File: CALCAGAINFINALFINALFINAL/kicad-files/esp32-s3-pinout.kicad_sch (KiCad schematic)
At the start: 1 part, among them U8 ESP32-S3-WROOM-1

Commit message: added 11pin expansion for accessories and micro-sd card slot
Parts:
- added H1, H2, H3, H4, H5: MountingHole_Pad, MountingHole:MountingHole_2.5mm_Pad, symbol Mechanical:MountingHole_Pad
- added J1: Conn_01x11_Socket, Connector_JST:JST_EH_B11B-EH-A_1x11_P2.50mm_Vertical, symbol Connector:Conn_01x11_Socket
- added J3: Micro_SD_Card, Connector_Card:microSD_HC_Molex_47219-2001, symbol Connector:Micro_SD_Card
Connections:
- net 3V3: now also J1.2 (Pin_2)
- net CS: now also H3.1
- net DC: now also H5.1
- net MOSI: now also H1.1, J1.6 (Pin_6)
- net RST: now also H4.1
- net SCK: now also H2.1, J1.8 (Pin_8)
- net SCL: now also J1.5 (Pin_5)
- net SDA: now also J1.4 (Pin_4)
- net GND: now reaches U8.1 (GND), U8.40 (GND), U8.41 (GND)
- net GND: now also J1.1 (Pin_1), J3.6 (VSS)
- net extra: now reaches U8.12 (IO8)
- net extra: now also J1.11 (Pin_11)
- net ~{INT}: now reaches U8.19 (IO11)
- net MISO: now reaches U8.22 (IO14)
- net MISO: now also J1.7 (Pin_7)
- net CS1: now reaches U8.8 (IO15)
- net CS1: now also J1.9 (Pin_9)
- net ~{INT1}: now reaches U8.9 (IO16)
- net ~{INT1}: now also J1.10 (Pin_10)
- new net VCC: J1.3 (Pin_3), J3.4 (VDD)
- no-connect marks 0 -> 1
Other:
- note added: "================================ J1 11-PIN EXPANSION PORT NOTES ================================ PINOUT MAPPING: - P1: GND | P7: MISO (IO14) [SPI Shared] - P2: 3V3 | P8: SCK (IO12) [SPI Shared] - P3: 5V (VBUS) | P9: CS1 (IO15) [Dedicated] - P4: SDA (IO7) | P10: IRQ (IO16) [Dedicated] - P5: SCL (IO6) | P11: TX (IO8) [Dedicated] - P6: MOSI(IO13) DESIGN & COEXISTENCE RULES: - SPI: Shares MOSI/SCK wi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"
- note added: "Display pins"

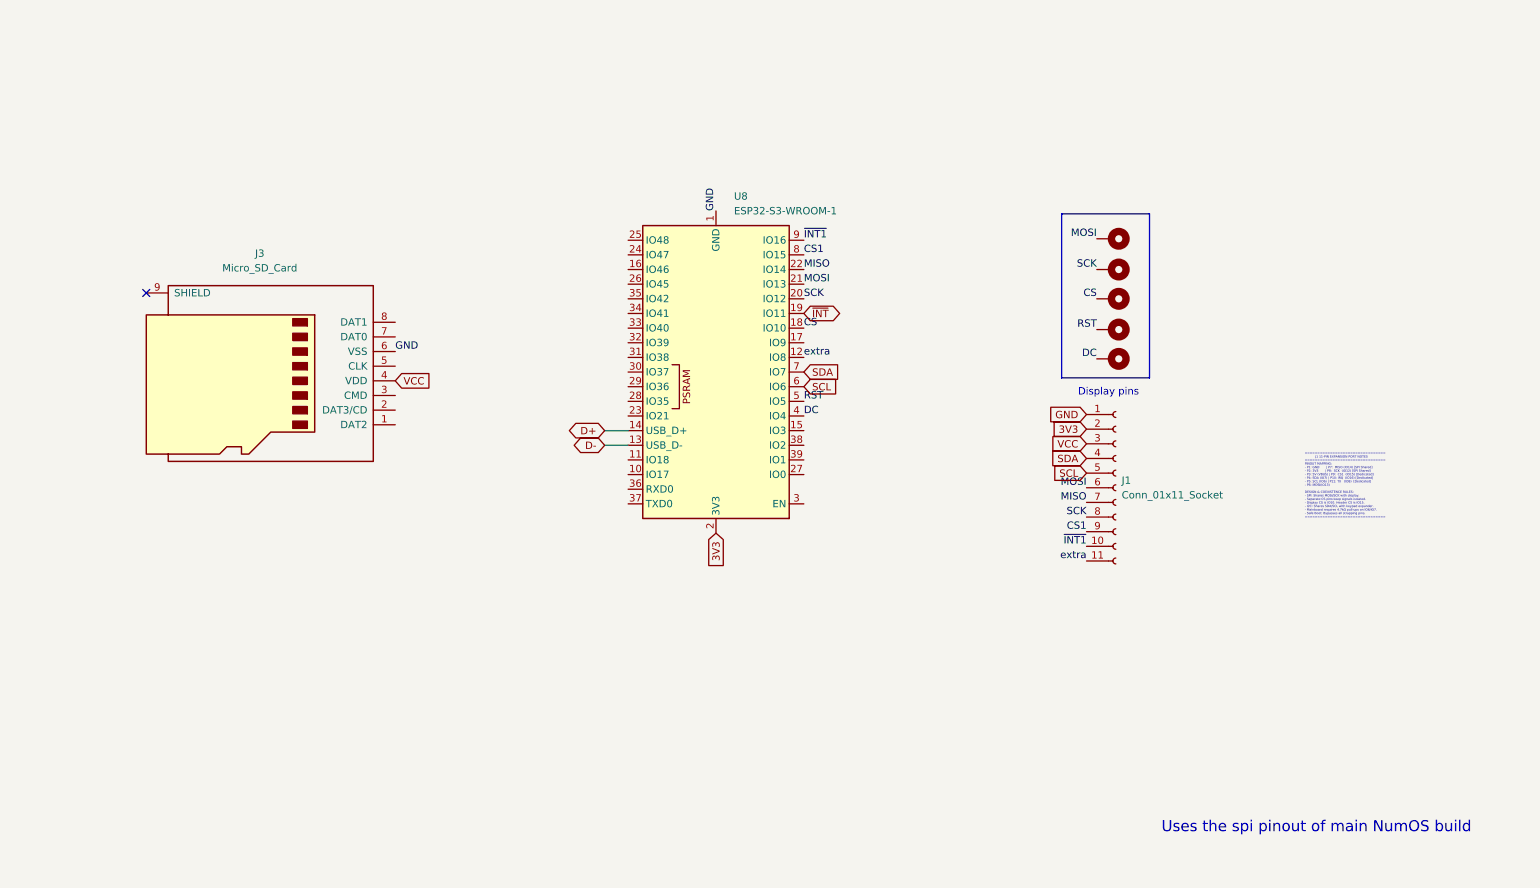
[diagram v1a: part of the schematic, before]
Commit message: Finished SD card and screen. Added camera connector and adjacent gpio expander
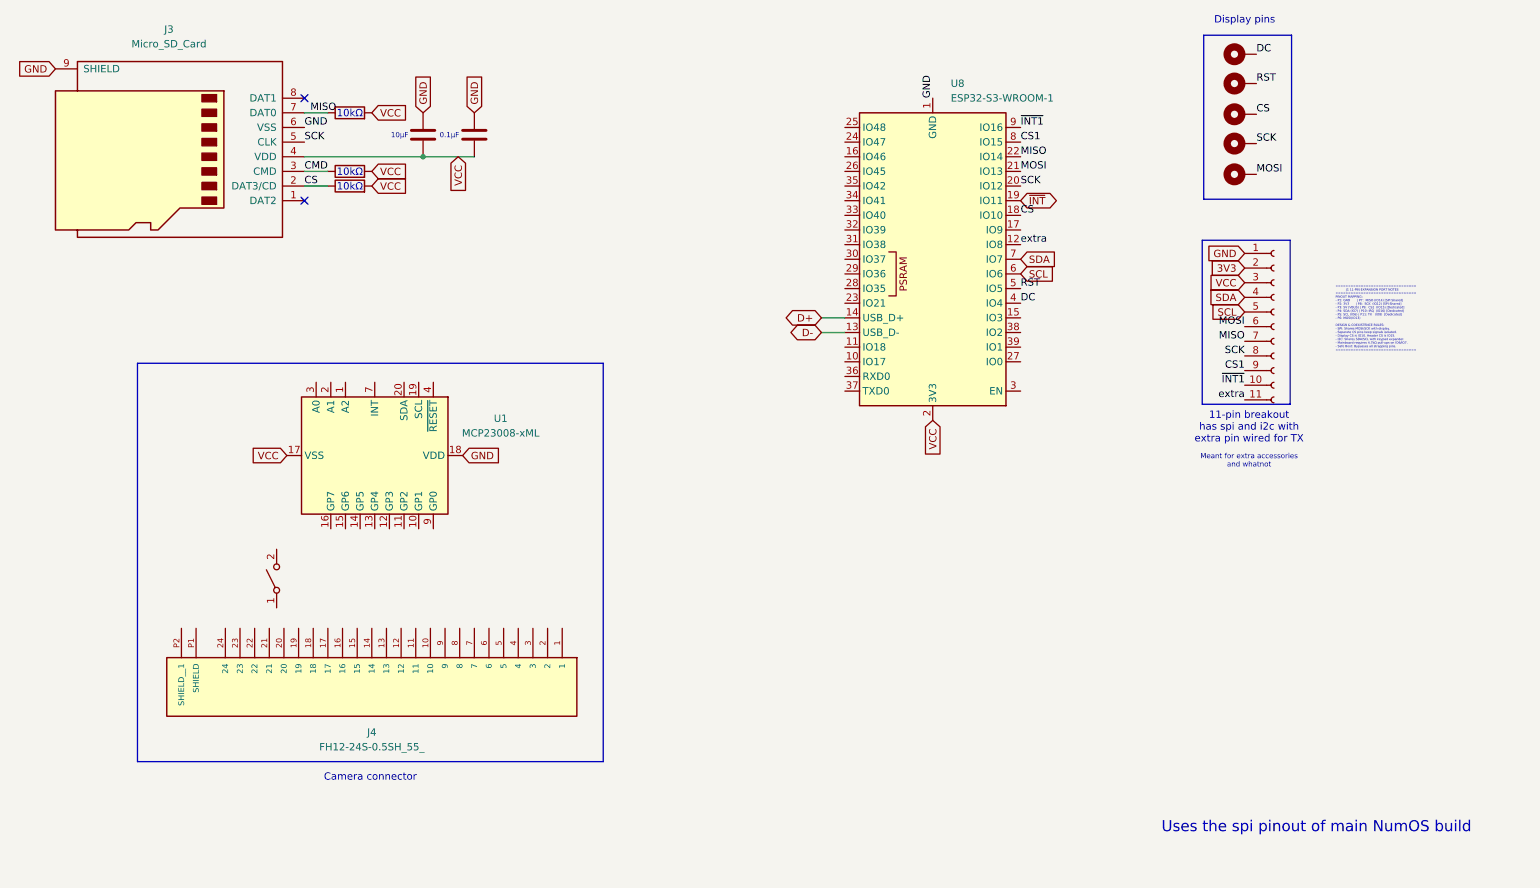
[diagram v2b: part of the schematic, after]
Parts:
- added C1, C2: C, symbol Device:C
- added J4: FH12-24S-0.5SH_55_, FH12-24S-0.5SH_55_:HRS_FH12-24S-0.5SH_55_, symbol FH12-24S-0.5SH_55_:FH12-24S-0.5SH_55_
- added R1, R2, R3: R, symbol Device:R
- added SW1: SW_SPST, symbol Switch:SW_SPST
- added U1: MCP23008-xML, Package_DFN_QFN:QFN-20-1EP_4x4mm_P0.5mm_EP2.7x2.7mm, symbol Interface_Expansion:MCP23008-xML
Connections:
- net 3V3: no longer U8.2 (3V3)
- net CS: now also J3.2 (DAT3/CD), R3.1
- net GND: now also J3.9 (SHIELD), C1.2, C2.2, U1.18 (VDD)
- net MISO: now also J3.7 (DAT0), R2.1
- net SCK: now also J3.5 (CLK)
- net VCC: now also U8.2 (3V3), C1.1, C2.1, R1.2, R2.2, R3.2, U1.17 (VSS)
- net CMD: now reaches J3.3 (CMD)
- net CMD: now also R1.1
- no-connect marks 1 -> 2
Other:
- note added: "0.1µF"
- note added: "10kΩ"
- note added: "10µF"
- note added: "11-pin breakout has spi and i2c with extra pin wired for TX"
- note added: "Camera connector"
- note added: "Meant for extra accessories and whatnot"
- moved on the sheet: J3, U8

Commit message: nearly finished with the no camera variant schematic stil have 2 drc warnings to fix but should be done in the next few hours.
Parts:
- removed J4: FH12-24S-0.5SH_55_, FH12-24S-0.5SH_55_:HRS_FH12-24S-0.5SH_55_, symbol FH12-24S-0.5SH_55_:FH12-24S-0.5SH_55_
- removed SW1: SW_SPST, symbol Switch:SW_SPST
- removed U1: MCP23008-xML, Package_DFN_QFN:QFN-20-1EP_4x4mm_P0.5mm_EP2.7x2.7mm, symbol Interface_Expansion:MCP23008-xML
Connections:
- net GND: now also J3.SH (SHIELD); no longer J3.9 (SHIELD)
- no-connect marks 2 -> 25
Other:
- note added: "SD card Slot"
- note added: "pin header for extra accessories and whatnot"
- note removed: "Camera connector"
- note removed: "Meant for extra accessories and whatnot"
- note removed: "Uses the spi pinout of main NumOS build"
- moved on the sheet: U8

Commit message: finalised no-camera branch. designing pcb then committing to origin/no-camera then tracing and adding camera to main
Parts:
- C1, C2: footprint (none) -> Capacitor_SMD:CP_Elec_3x5.3
- R1, R2, R3: footprint (none) -> Resistor_SMD:R_0201_0603Metric
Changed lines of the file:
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@@
 			)
 		)
-		(property "Footprint" ""
+		(property "Footprint" "Resistor_SMD:R_0201_0603Metric"
 			(at 77.724 47.244 90)
 			(hide yes)
@@
 			)
 		)
-		(property "Footprint" ""
+		(property "Footprint" "Capacitor_SMD:CP_Elec_3x5.3"
 			(at 98.3488 35.306 0)
 			(hide yes)
@@
 			)
 		)
-		(property "Footprint" ""
+		(property "Footprint" "Capacitor_SMD:CP_Elec_3x5.3"
 			(at 89.4588 35.306 0)
 			(hide yes)
@@
 			)
 		)
-		(property "Footprint" ""
+		(property "Footprint" "Resistor_SMD:R_0201_0603Metric"
 			(at 77.724 37.084 90)
 			(hide yes)
@@
 			)
 		)
-		(property "Footprint" ""
+		(property "Footprint" "Resistor_SMD:R_0201_0603Metric"
 			(at 77.724 49.784 90)
 			(hide yes)

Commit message: dude this bitch ass project is the fucking boulder of sisyphus omfg ima genuinely kms at this rate if this iteration doesnt work ima genuinely kms like acutal this one is bare esp32 s3 with a diy antenna and crystal like dude what the actual fuck man ima genuinely dei. FINAL FINAL FINAL FINAL ITS GOT THE FUCKING BARE CHIPS FOR DAMN NEAR EVERYTHING DEAR MASS PRODUCED CHINK FACTORY GODS LET THIS THROUGH WITHOUT CAUSING A RUCKUS AND CHARGING LIKE $90 FOR 14 BUCKS OF PARTS AMEN
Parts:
- removed J1: Conn_01x11_Socket, Connector_JST:JST_EH_B11B-EH-A_1x11_P2.50mm_Vertical, symbol Connector:Conn_01x11_Socket
- removed U8: ESP32-S3-WROOM-1, RF_Module:ESP32-S3-WROOM-1, symbol RF_Module:ESP32-S3-WROOM-1
- added U1: ESP32-S3, Package_DFN_QFN:QFN-56-1EP_7x7mm_P0.4mm_EP4x4mm, symbol MCU_Espressif:ESP32-S3
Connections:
- net D+: now also U1.26 (GPIO20/USB_D+)
- net D-: now also U1.25 (GPIO19/USB_D-)
- net GND: now also U1.57 (GND)
- new net: U1.2 (VDD3P3), U1.3 (VDD3P3)
- new net: U1.55 (VDDA), U1.56 (VDDA)
- no-connect marks 25 -> 30
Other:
- note added: "==================================================================== ILI9341 40-PIN DISPLAY TO ESP32-S3 WROOM-1 WIRING LOG (4-WIRE SPI) ==================================================================== [POWER & GROUND] -------------------------------------------------------------------- Display Pin 5 (GND) --> Connect to GND Display Pin 6 (IOVCC) --> Connect to 3.3V Power Rail Display Pin 16 (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"
- note removed: "11-pin breakout has spi and i2c with extra pin wired for TX"
- note removed: "================================ J1 11-PIN EXPANSION PORT NOTES ================================ PINOUT MAPPING: - P1: GND | P7: MISO (IO14) [SPI Shared] - P2: 3V3 | P8: SCK (IO12) [SPI Shared] - P3: 5V (VBUS) | P9: CS1 (IO15) [Dedicated] - P4: SDA (IO7) | P10: IRQ (IO16) [Dedicated] - P5: SCL (IO6) | P11: TX (IO8) [Dedicated] - P6: MOSI(IO13) DESIGN & COEXISTENCE RULES: - SPI: Shares MOSI/SCK wi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"
- note removed: "pin header for extra accessories and whatnot"

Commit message: I reckon its all done now. need to doucble check all pin assignments tomorrow and then add camera then order everything. we might lowkirkenuinely launch this shit chat
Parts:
- removed U1: ESP32-S3, Package_DFN_QFN:QFN-56-1EP_7x7mm_P0.4mm_EP4x4mm, symbol MCU_Espressif:ESP32-S3
- added U8: ESP32-S3-WROOM-1, RF_Module:ESP32-S3-WROOM-1, symbol RF_Module:ESP32-S3-WROOM-1
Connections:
- net CS: now also U8.18 (IO10)
- net CS1: now also U8.8 (IO15)
- net D+: now also U8.14 (USB_D+)
- net D-: now also U8.13 (USB_D-)
- net DC: now also U8.4 (IO4)
- net GND: now also U8.1 (GND), U8.40 (GND), U8.41 (GND)
- net MISO: now also U8.22 (IO14)
- net MOSI: now also U8.21 (IO13)
- net RST: now also U8.5 (IO5)
- net SCK: now also U8.20 (IO12)
- net SCL: now also U8.6 (IO6)
- net SDA: now also U8.7 (IO7)
- net VCC: now also U8.2 (3V3)
- net extra: now also U8.12 (IO8)
- net ~{INT1}: now also U8.9 (IO16)
- net ~{INT}: now also U8.19 (IO11)
- no-connect marks 30 -> 25

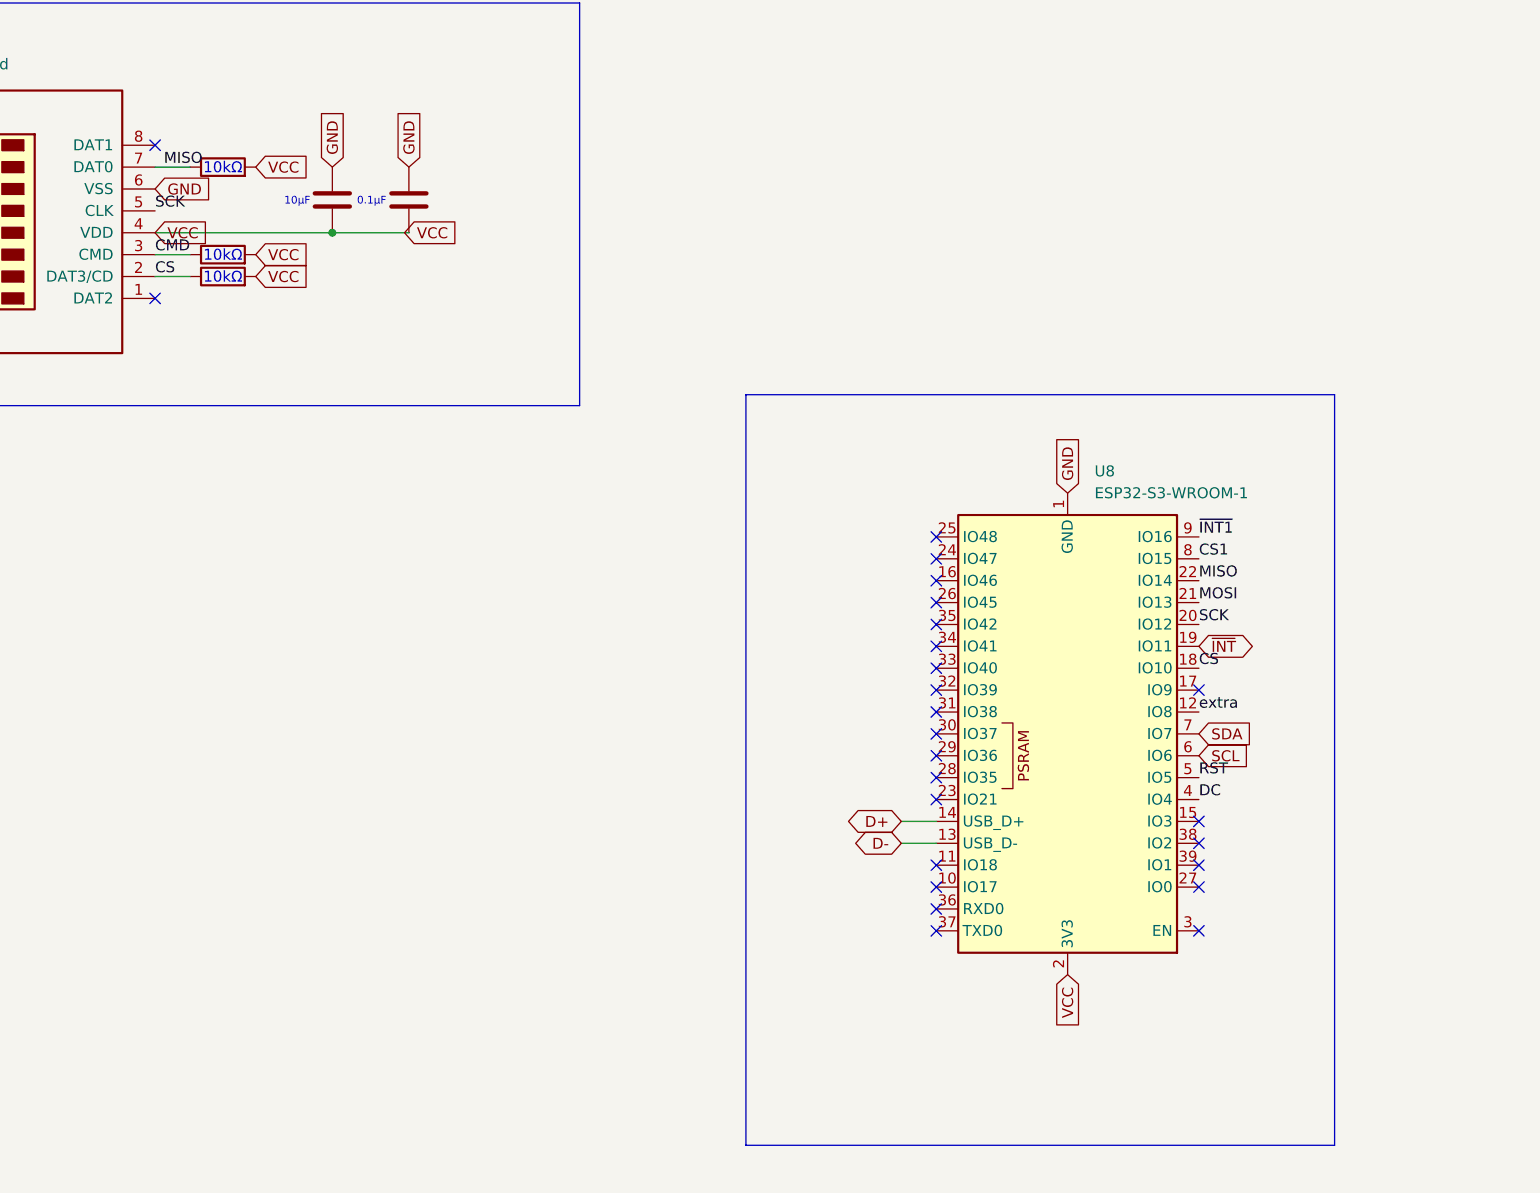
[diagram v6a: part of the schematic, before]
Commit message: finalised pcb w camera. thing is im kinda poor rn and ill prob get enough money to order pcba after 2 weeks. until then ima js focus on school and get thru to working on tweaking the HAL and ui to match my spec and the design language of ABSOLUT-CAS
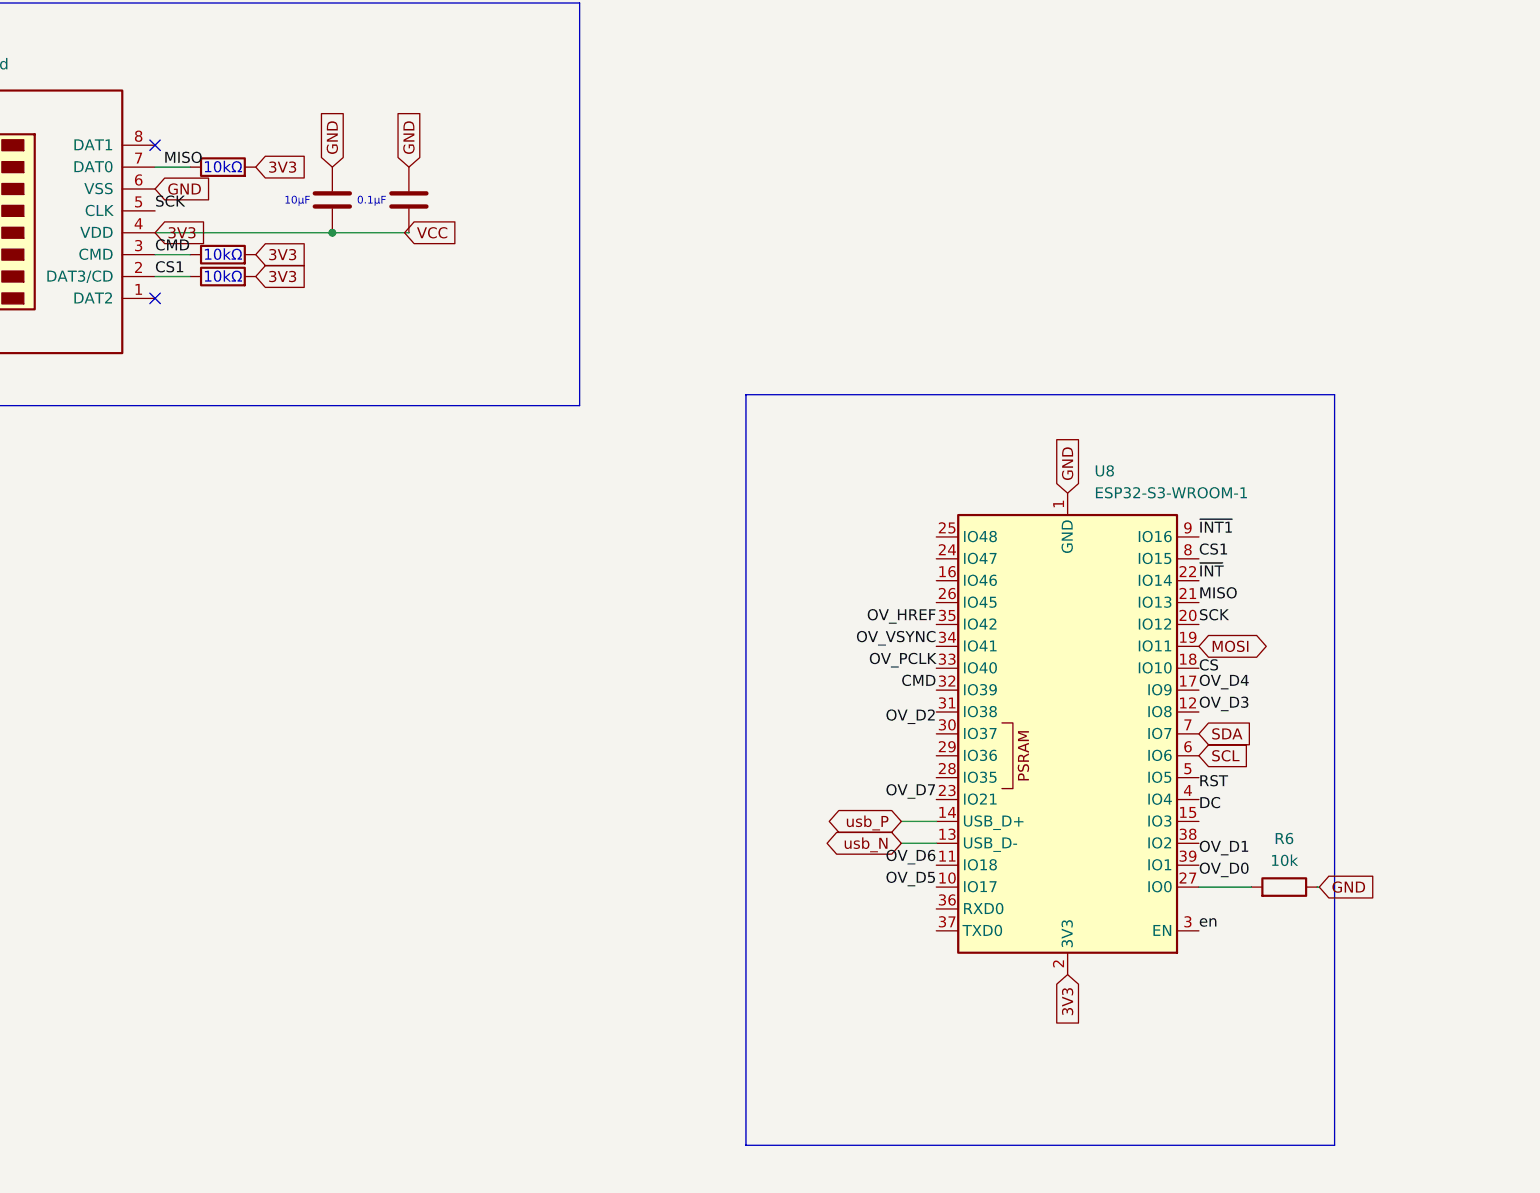
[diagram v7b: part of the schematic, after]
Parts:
- added R6: 10k, symbol Device:R
- C1: value C -> 0.1; footprint Capacitor_SMD:CP_Elec_3x5.3 -> Capacitor_SMD:C_0603_1608Metric; KiLib_Generator (none) -> SMD_2terminal_chip_molded; LCSC (none) -> C1525
- C2: value C -> 10uf; footprint Capacitor_SMD:CP_Elec_3x5.3 -> Capacitor_SMD:C_0603_1608Metric; KiLib_Generator (none) -> SMD_2terminal_chip_molded; LCSC (none) -> C7171
- J3: LCSC (none) -> C91145
- R1, R3: KiLib_Generator (none) -> SMD_2terminal_chip_molded; LCSC (none) -> C17414
- R2: value R -> 10k; KiLib_Generator (none) -> SMD_2terminal_chip_molded; LCSC (none) -> C17414
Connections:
- net CMD: now also U8.32 (IO39)
- net CS: no longer J3.2 (DAT3/CD), R3.1
- net CS1: now also J3.2 (DAT3/CD), R3.1
- net GND: now also R6.1
- net MISO: now also U8.21 (IO13); no longer U8.22 (IO14)
- net MOSI: now also U8.19 (IO11); no longer U8.21 (IO13)
- net ~{INT}: now also U8.22 (IO14); no longer U8.19 (IO11)
- net OV_D5: now reaches U8.10 (IO17)
- net OV_D6: now reaches U8.11 (IO18)
- net OV_D4: now reaches U8.17 (IO9)
- net OV_D7: now reaches U8.23 (IO21)
- net at U8.27 (IO0): now also R6.2
- net en: now reaches U8.3 (EN)
- net OV_D2: now reaches U8.31 (IO38)
- net OV_PCLK: now reaches U8.33 (IO40)
- net OV_VSYNC: now reaches U8.34 (IO41)
- net OV_HREF: now reaches U8.35 (IO42)
- net OV_D1: now reaches U8.38 (IO2)
- net OV_D0: now reaches U8.39 (IO1)
- net D+ renamed usb_P
- net D- renamed usb_N
- net VCC renamed 3V3
- net extra renamed OV_D3
- no-connect marks 25 -> 2
